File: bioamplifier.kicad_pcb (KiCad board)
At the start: 4 copper layers, 54.5 x 54.7 mm, 65 parts, among them J1 Conn_01x40_Pin, J2 Conn_01x26_Pin, U1 ADS1299IPAG, U10 TPD4E1B06DCKR, U2 TPD4E1B06DCKR, U3 TPD4E1B06DCKR, U4 TPD4E1B06DCKR, U5 TPD4E1B06DCKR, U7 TPS73133DBV, U8 TPS73201DCQ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

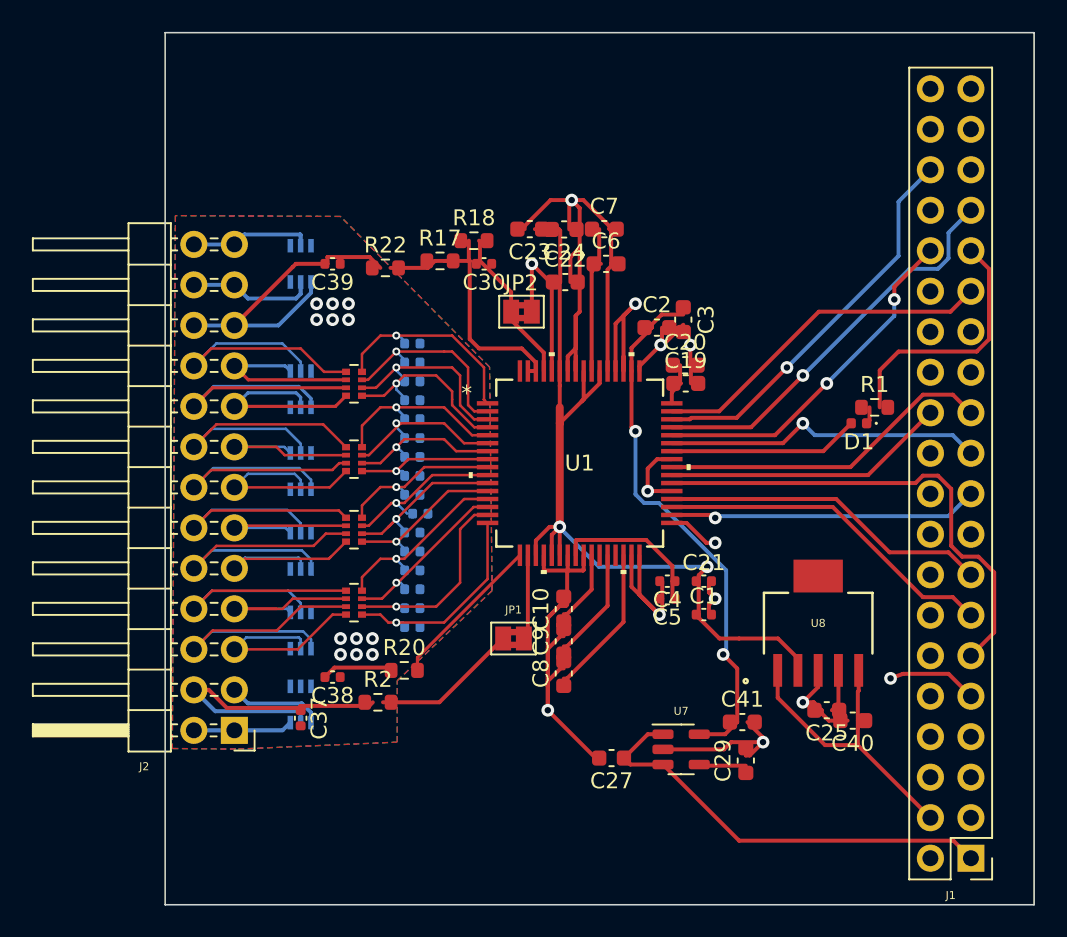
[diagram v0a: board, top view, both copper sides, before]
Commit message: redone analog inputs, adjusted all footprints to match real components, added library for potential implementation of 4 element capacitor arrays
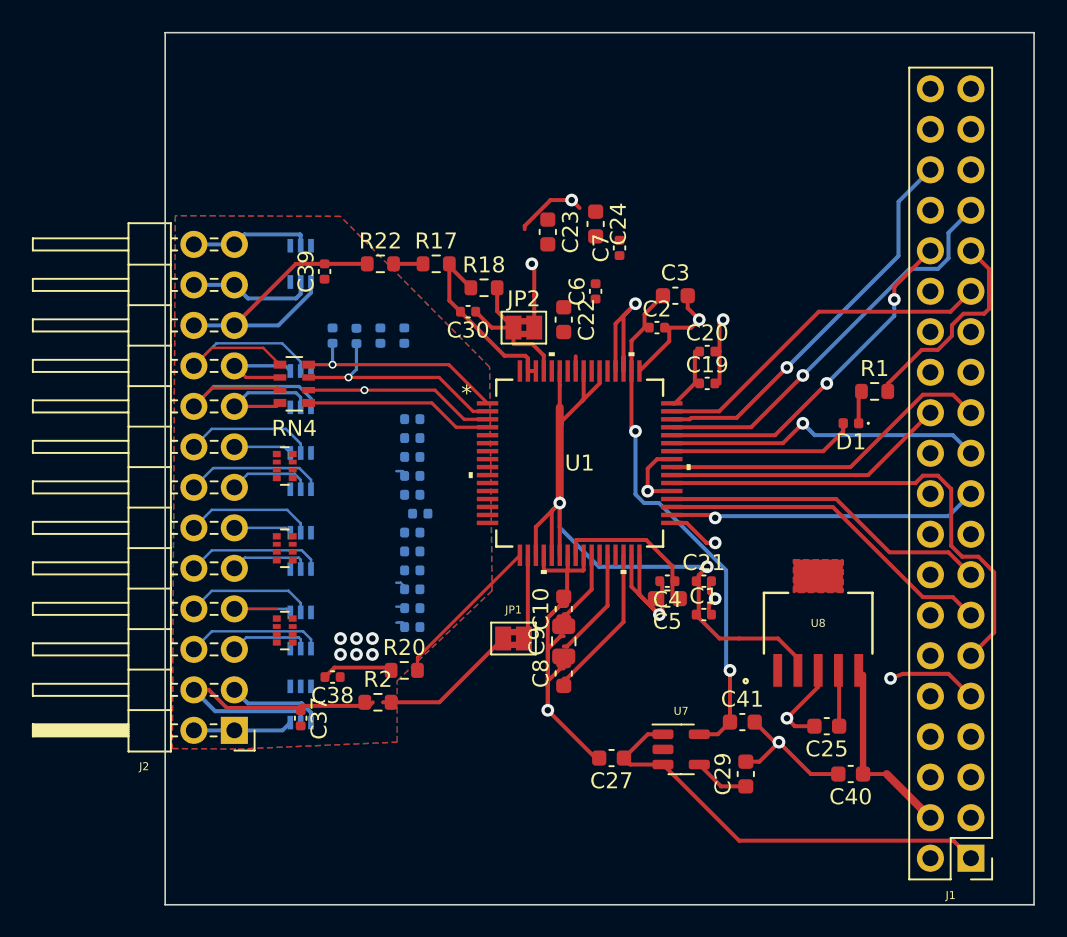
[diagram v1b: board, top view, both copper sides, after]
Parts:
- C11, C12, C13, C14, C15, C16, C17, C18, C26, C28, C31, C32, C33, C34, C35, C36, C37, C38, C39: value 6.8 uF -> 1 nF
- C19, C2, C20, C6, C7: footprint Capacitor_SMD:C_0603_1608Metric -> Capacitor_SMD:C_0402_1005Metric
- C5: footprint Capacitor_SMD:C_0402_1005Metric -> Capacitor_SMD:C_0603_1608Metric
- C9: footprint Capacitor_SMD:C_0603_1608Metric -> Capacitor_SMD:C_0805_2012Metric
- RN4: footprint Resistor_SMD:R_Array_Convex_4x0402 -> Resistor_SMD:R_Array_Convex_4x0603
- moved C33 5.02 mm to (63.5, 80.5), turned to -90 degrees
- moved RN1 4.68 mm to (60.5, 99.0)
- moved RN3 4.50 mm to (60.5, 93.8)
- moved RN2 4.37 mm to (60.5, 88.7)
- moved C17 4.09 mm to (68.0, 80.5), turned to -90 degrees
- moved C32 3.88 mm to (65.0, 80.5), turned to -90 degrees
- moved RN4 3.74 mm to (61.1, 83.5)
- moved C18 3.50 mm to (66.5, 80.5), turned to -90 degrees
- moved C40 3.35 mm to (96.0, 108.0)
- moved C30 3.16 mm to (72.0, 79.0)
- moved R18 3.02 mm to (73.0, 77.5)
- moved C22 2.36 mm to (78.0, 79.5), turned to -90 degrees
- moved C24 2.00 mm to (80.0, 73.5), turned to -90 degrees
- moved C6 1.85 mm to (80.0, 77.7), turned to 90 degrees
- moved C20 1.63 mm to (87.0, 81.5)
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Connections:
- U1 pad 18: Net-(JP1-B) -> SRB2
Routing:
- net GNDA: track 109.4 -> 71.7 mm, vias 19 -> 13
- net IN1P: track 13.5 -> 0.80 mm, vias 1 -> 0
- net IN1N: track 12.9 -> 0.72 mm, vias 1 -> 0
- net IN2N: track 11.8 -> 0.00 mm, vias 1 -> 0
- net IN6N: track 11.4 -> 0.00 mm, vias 1 -> 0
- net IN3N: track 11.0 -> 0.00 mm, vias 1 -> 0
- net /Electrodes input/N6: track 18.9 -> 8.14 mm
- net /Electrodes input/N1: track 19.3 -> 8.61 mm
- net IN4N: track 10.5 -> 0.00 mm, vias 1 -> 0
- net /Electrodes input/N3: track 19.1 -> 8.64 mm
- net IN6P: track 10.4 -> 0.00 mm, vias 1 -> 0
- net IN2P: track 11.1 -> 0.85 mm, vias 1 -> 0
- net /Electrodes input/N4: track 18.3 -> 8.10 mm
- net /Electrodes input/N5: track 18.9 -> 8.74 mm
- net IN4P: track 10.1 -> 0.00 mm, vias 1 -> 0
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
